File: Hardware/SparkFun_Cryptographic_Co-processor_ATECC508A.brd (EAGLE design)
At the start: 25.4 x 25.4 mm, 40 parts, among them J1 QWIIC, J2 QWIIC, J3 PTH, U1 ATECC508A

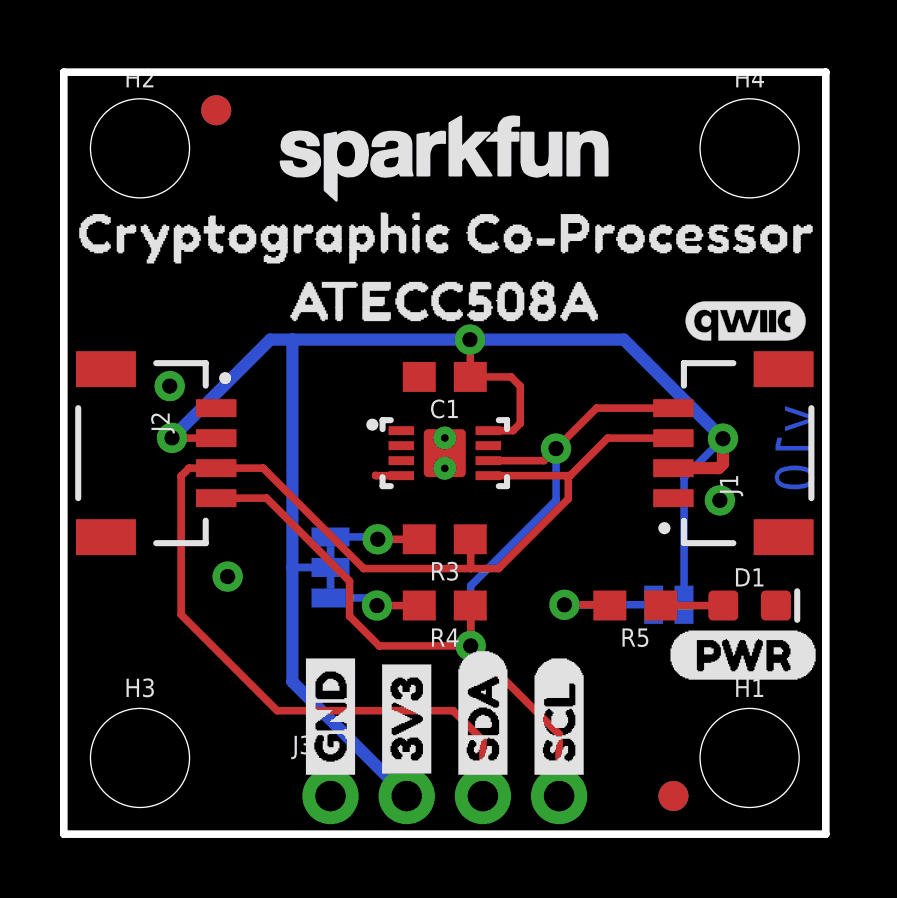
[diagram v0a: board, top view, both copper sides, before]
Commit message: silk on jumpers, rotate I2C jumper label, changed name on symbols to match
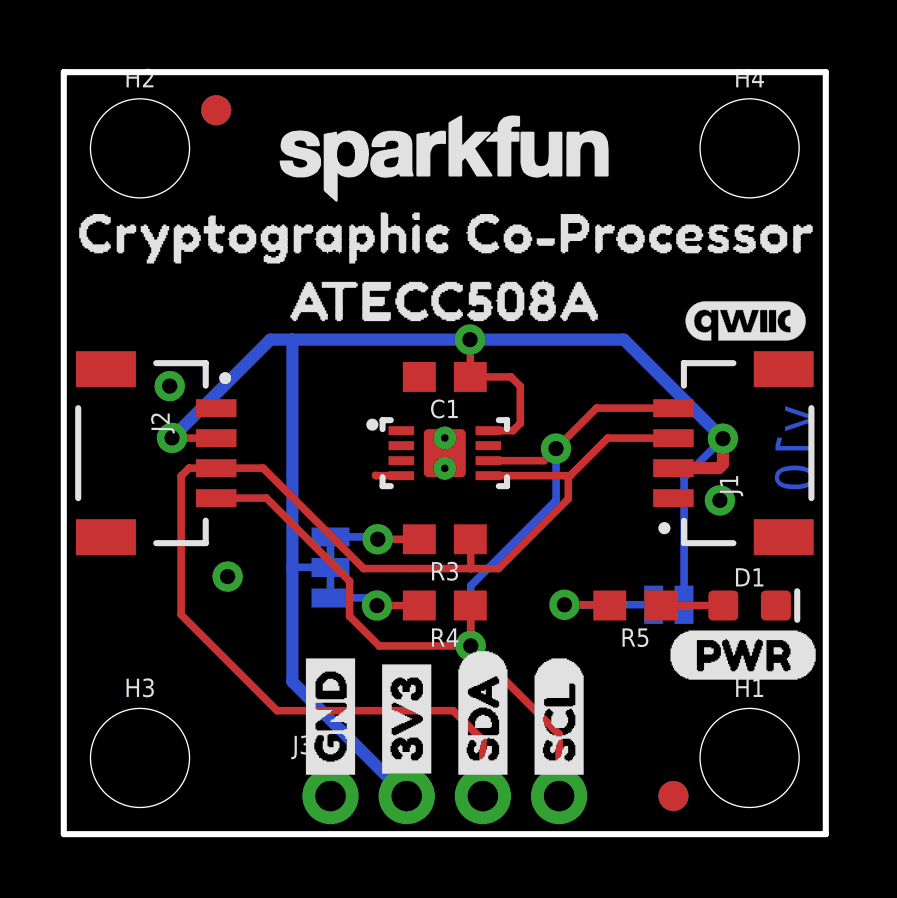
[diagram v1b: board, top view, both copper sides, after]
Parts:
- removed JP1: (no value), SparkFun-Jumpers:SMT-JUMPER_2_NC_TRACE_NO-SILK
- removed JP4: (no value), SparkFun-Jumpers:SMT-JUMPER_3_2-NC_TRACE_NO-SILK
- added I2C: (no value), SparkFun-Jumpers:SMT-JUMPER_3_2-NC_TRACE_SILK
- added LED: (no value), SparkFun-Jumpers:SMT-JUMPER_2_NC_TRACE_SILK
- moved LOGO4 10.6 mm to (22.5, 16.6)
- moved U$22 3.65 mm to (11.0, 11.4), turned to 0 degrees
- moved U$1 0.23 mm to (22.5, 9.42)
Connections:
- net 3.3V: now also I2C.2, LED.2; no longer JP1.2, JP4.2
- net N$4: now also I2C.3; no longer JP4.3
- net N$5: now also I2C.1; no longer JP4.1
- net N$7: now also LED.1; no longer JP1.1

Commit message: Design review changes - silk, sch, prod id - ready for reds
-added sweet key graphic
-added default I2C address to sch
-added PROD ID to part in library. (note, still need to migrate to official libraries when this goes live).
-added NC pin to symbol/dev for IC.
-nudges a via and some traces to line up with key graphic hole
-rotated LED label to match others' orientation.
-swapped jumper packages to include silk outlines
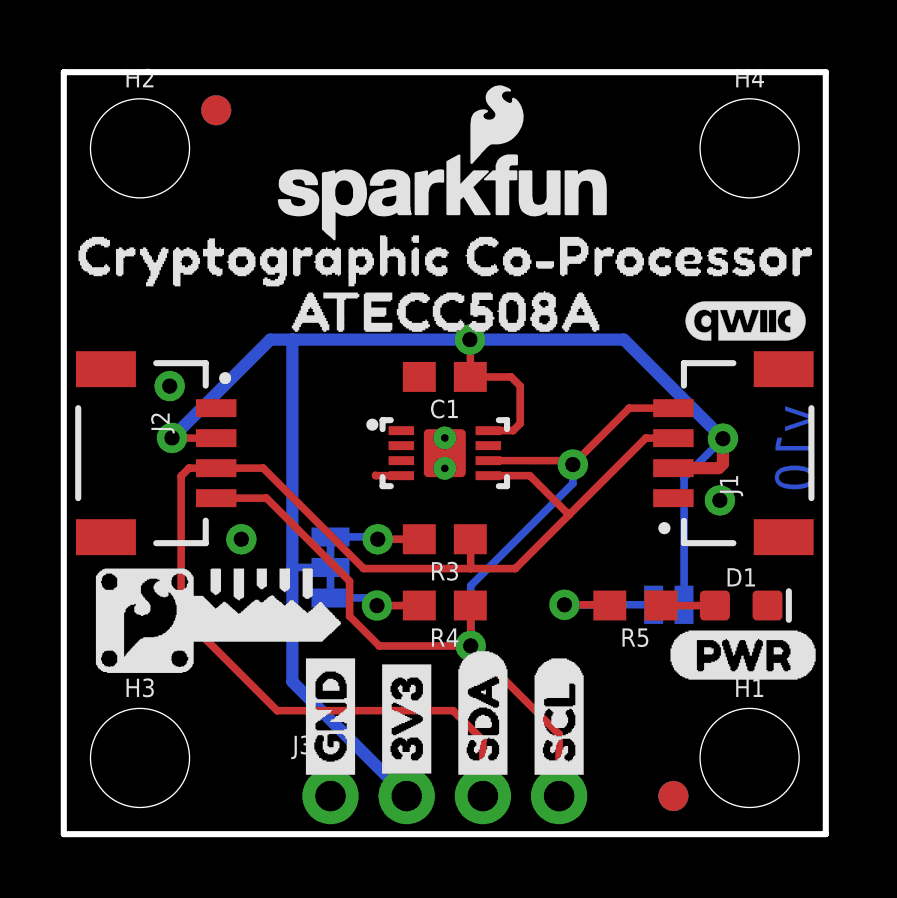
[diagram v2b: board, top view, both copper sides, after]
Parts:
- removed U$9: (no value), SparkFun-Aesthetics:QWIIC_4MM
- added U$15: (no value), crypto_coprocessor_logo#04#png (1):CRYPTO_COPROCESSOR_LOGO#04#PNG
- added U$18: (no value), crypto_coprocessor_logo#04#png (2):CRYPTO_COPROCESSOR_LOGO#04#PNG
- LOGO1, LOGO2: value SFE_LOGO_NAME.1_INCH -> SFE_LOGO_NAME_FLAME.1_INCH; device SparkFun-Aesthetics:SFE_LOGO_NAME_.1 -> SparkFun-Aesthetics:SFE_LOGO_NAME_FLAME_.1
- moved LOGO4 22.6 mm to (2.54, 6.10)
- moved LOGO1 1.27 mm to (12.7, 21.3)
- moved LOGO2 1.27 mm to (12.7, 21.3)
- moved U$17 0.76 mm to (-0.71, 19.3)
- moved U$11 0.72 mm to (26.1, 19.3)
- moved U$14 0.39 mm to (19.1, 17.4)
- moved U$12 0.36 mm to (6.40, 17.4)
- moved D1 0.28 mm to (22.6, 7.62)
